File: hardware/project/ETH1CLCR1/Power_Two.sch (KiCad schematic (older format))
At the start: 53 parts, among them U1501 LT8330_S6, U1502 LT8330_S6, U1503 MC7815BD2TG, U1504 MC7915BD2TG, U1505 MC78M12ABDTRKG, U1506 MC79M12CDTG, U1507 TSR2-2450, U1508 TSR1-2490, U1509 LM1117IMP-3.3/NOPB, U1510 LM1117IMP-3.3/NOPB, U1511 LM1117IMP-5.0/NOPB

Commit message: PCB layout
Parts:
- R1506: value R -> 97k6
- R1508: value R -> 46k4
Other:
- moved on the sheet: C1501, C1502, C1503, C1504, C1505, C1506, C1507, C1508, C1509, C1510, C1511, C1512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

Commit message: Changes in schematics.
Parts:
- C1510, C1512: value 2u2/50V -> 4u7/50V
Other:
- moved on the sheet: TP1501
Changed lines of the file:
@@
 encoding utf-8
 Sheet 15 15
-Title ""
-Date ""
-Rev ""
+Title "Power supply second"
+Date "2020-01-19"
+Rev "1.0"
 Comp ""
-Comment1 ""
+Comment1 "Verification done."
 Comment2 ""
 Comment3 ""
@@
 Wire Wire Line
 	6500 1000 6550 1000
-Wire Wire Line
-	6550 1450 6550 1400
 $Comp
 L Device:R R1505
@@
 Wire Wire Line
 	6500 3350 6550 3350
-Wire Wire Line
-	6550 3800 6550 3750
 $Comp
 L Device:R R1507
@@
 P 8150 3800
 F 0 "C1510" H 8265 3846 50  0000 L CNN
-F 1 "2u2/50V" H 8265 3755 50  0000 L CNN
+F 1 "4u7/50V" H 8265 3755 50  0000 L CNN
 F 2 "Capacitor_SMD:C_1206_3216Metric_Pad1.42x1.75mm_HandSolder" H 8188 3650 50  0001 C CNN
 F 3 "~" H 8150 3800 50  0001 C CNN
@@
 P 8750 3800
 F 0 "C1512" H 8865 3846 50  0000 L CNN
-F 1 "2u2/50V" H 8865 3755 50  0000 L CNN
+F 1 "4u7/50V" H 8865 3755 50  0000 L CNN
 F 2 "Capacitor_SMD:C_1206_3216Metric_Pad1.42x1.75mm_HandSolder" H 8788 3650 50  0001 C CNN
 F 3 "~" H 8750 3800 50  0001 C CNN
@@
 L ETH1CLCR1:DGNDF #PWR01509
 U 1 1 5DF487C8
-P 6550 1450
-F 0 "#PWR01509" H 6550 1200 50  0001 C CNN
-F 1 "DGNDF" H 6555 1277 50  0000 C CNN
-F 2 "" H 6550 1450 50  0001 C CNN
-F 3 "" H 6550 1450 50  0001 C CNN
-	1    6550 1450
+P 6550 1400
+F 0 "#PWR01509" H 6550 1150 50  0001 C CNN
+F 1 "DGNDF" H 6555 1227 50  0000 C CNN
+F 2 "" H 6550 1400 50  0001 C CNN
+F 3 "" H 6550 1400 50  0001 C CNN
+	1    6550 1400
 	1    0    0    -1
 $EndComp
@@
 L ETH1CLCR1:DGNDF #PWR01510
 U 1 1 5F7AA41C
-P 6550 3800
-F 0 "#PWR01510" H 6550 3550 50  0001 C CNN
-F 1 "DGNDF" H 6555 3627 50  0000 C CNN
-F 2 "" H 6550 3800 50  0001 C CNN
-F 3 "" H 6550 3800 50  0001 C CNN
-	1    6550 3800
+P 6550 3750
+F 0 "#PWR01510" H 6550 3500 50  0001 C CNN
+F 1 "DGNDF" H 6555 3577 50  0000 C CNN
+F 2 "" H 6550 3750 50  0001 C CNN
+F 3 "" H 6550 3750 50  0001 C CNN
+	1    6550 3750
 	1    0    0    -1
 $EndComp
@@
 L Connector:TestPoint TP?
 U 1 1 5E1A35BB
-P 900 900
+P 900 800
 AR Path="/5DF36C0B/5E1A35BB" Ref="TP?"  Part="1"
 AR Path="/5DD0DBE6/5E1A35BB" Ref="TP?"  Part="1"
 AR Path="/5DEC0296/5E1A35BB" Ref="TP1501"  Part="1"
-F 0 "TP1501" H 958 1018 50  0000 L CNN
-F 1 "5006" H 958 927 50  0000 L CNN
-F 2 "TestPoint:TestPoint_Loop_D2.60mm_Drill1.6mm_Beaded" H 1100 900 50  0001 C CNN
-F 3 "~" H 1100 900 50  0001 C CNN
-	1    900  900
+F 0 "TP1501" H 958 918 50  0000 L CNN
+F 1 "5006" H 958 827 50  0000 L CNN
+F 2 "TestPoint:TestPoint_Loop_D2.60mm_Drill1.6mm_Beaded" H 1100 800 50  0001 C CNN
+F 3 "~" H 1100 800 50  0001 C CNN
+	1    900  800
 	1    0    0    -1
 $EndComp
@@
 L ETH1CLCR1:DGNDF #PWR01503
 U 1 1 5E1AEE0F
-P 900 1000
-F 0 "#PWR01503" H 900 750 50  0001 C CNN
-F 1 "DGNDF" H 905 827 50  0000 C CNN
-F 2 "" H 900 1000 50  0001 C CNN
-F 3 "" H 900 1000 50  0001 C CNN
-	1    900  1000
-	1    0    0    -1
-$EndComp
-Wire Wire Line
-	900  1000 900  900
+P 900 900
+F 0 "#PWR01503" H 900 650 50  0001 C CNN
+F 1 "DGNDF" H 905 727 50  0000 C CNN
+F 2 "" H 900 900 50  0001 C CNN
+F 3 "" H 900 900 50  0001 C CNN
+	1    900  900
+	1    0    0    -1
+$EndComp
+Wire Wire Line
+	900  900  900  800
 $Comp
 L power:PWR_FLAG #FLG01504
@@
 L ETH1CLCR1:+24VF #PWR01518
 U 1 1 5E91BD20
-P 3300 850
-F 0 "#PWR01518" H 3300 700 50  0001 C CNN
-F 1 "+24VF" H 3315 1023 50  0000 C CNN
-F 2 "" H 3300 850 50  0001 C CNN
-F 3 "" H 3300 850 50  0001 C CNN
-	1    3300 850
+P 2650 800
+F 0 "#PWR01518" H 2650 650 50  0001 C CNN
+F 1 "+24VF" H 2665 973 50  0000 C CNN
+F 2 "" H 2650 800 50  0001 C CNN
+F 3 "" H 2650 800 50  0001 C CNN
+	1    2650 800
 	1    0    0    -1
 $EndComp
@@
 L ETH1CLCR1:+24VDD #PWR01517
 U 1 1 5E91C38B
-P 2850 850
-F 0 "#PWR01517" H 2850 700 50  0001 C CNN
-F 1 "+24VDD" H 2865 1023 50  0000 C CNN
-F 2 "" H 2850 850 50  0001 C CNN
-F 3 "" H 2850 850 50  0001 C CNN
-	1    2850 850
-	1    0    0    -1
-$EndComp
-Wire Wire Line
-	2850 850  2850 900
-Wire Wire Line
-	2850 900  3300 900
-Wire Wire Line
-	3300 900  3300 850
+P 2200 800
+F 0 "#PWR01517" H 2200 650 50  0001 C CNN
+F 1 "+24VDD" H 2215 973 50  0000 C CNN
+F 2 "" H 2200 800 50  0001 C CNN
+F 3 "" H 2200 800 50  0001 C CNN
+	1    2200 800
+	1    0    0    -1
+$EndComp
+Wire Wire Line
+	2200 800  2200 850
+Wire Wire Line
+	2200 850  2650 850
+Wire Wire Line
+	2650 850  2650 800
 $Comp
 L ETH1CLCR1:DGNDF #PWR01504
 U 1 1 5E95CC6A
-P 1900 1000
-F 0 "#PWR01504" H 1900 750 50  0001 C CNN
-F 1 "DGNDF" H 1905 827 50  0000 C CNN
-F 2 "" H 1900 1000 50  0001 C CNN
-F 3 "" H 1900 1000 50  0001 C CNN
-	1    1900 1000
+P 1350 900
+F 0 "#PWR01504" H 1350 650 50  0001 C CNN
+F 1 "DGNDF" H 1355 727 50  0000 C CNN
+F 2 "" H 1350 900 50  0001 C CNN
+F 3 "" H 1350 900 50  0001 C CNN
+	1    1350 900
 	1    0    0    -1
 $EndComp
@@
 L ETH1CLCR1:AGNDF #PWR01505
 U 1 1 5E95D4F1
-P 2250 1000
-F 0 "#PWR01505" H 2250 750 50  0001 C CNN
-F 1 "AGNDF" H 2255 827 50  0000 C CNN
-F 2 "" H 2250 1000 50  0001 C CNN
-F 3 "" H 2250 1000 50  0001 C CNN
-	1    2250 1000
-	1    0    0    -1
-$EndComp
-Wire Wire Line
-	2250 1000 2250 950
-Wire Wire Line
-	2250 950  1900 950
-Wire Wire Line
-	1900 950  1900 1000
+P 1700 900
+F 0 "#PWR01505" H 1700 650 50  0001 C CNN
+F 1 "AGNDF" H 1705 727 50  0000 C CNN
+F 2 "" H 1700 900 50  0001 C CNN
+F 3 "" H 1700 900 50  0001 C CNN
+	1    1700 900
+	1    0    0    -1
+$EndComp
+Wire Wire Line
+	1700 900  1700 850
+Wire Wire Line
+	1700 850  1350 850
+Wire Wire Line
+	1350 850  1350 900
 $Comp
 L power:GND #PWR01508
 U 1 1 5EA5587E
-P 2600 1000
-F 0 "#PWR01508" H 2600 750 50  0001 C CNN
-F 1 "GND" H 2605 827 50  0000 C CNN
-F 2 "" H 2600 1000 50  0001 C CNN
-F 3 "" H 2600 1000 50  0001 C CNN
-	1    2600 1000
-	1    0    0    -1
-$EndComp
-Wire Wire Line
-	2250 950  2600 950
-Wire Wire Line
-	2600 950  2600 1000
-Connection ~ 2250 950
+P 2050 900
+F 0 "#PWR01508" H 2050 650 50  0001 C CNN
+F 1 "GND" H 2055 727 50  0000 C CNN
+F 2 "" H 2050 900 50  0001 C CNN
+F 3 "" H 2050 900 50  0001 C CNN
+	1    2050 900
+	1    0    0    -1
+$EndComp
+Wire Wire Line
+	1700 850  2050 850
+Wire Wire Line
+	2050 850  2050 900
+Connection ~ 1700 850
 $EndSCHEMATC

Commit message: Checked the schematics. Created BOM.
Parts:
- U1509, U1510: value LM1117IMP-3.3/NOPB -> LM1117DTX-3.3/NOPB
- U1511: value LM1117IMP-5.0/NOPB -> LM1117DTX-5.0/NOPB
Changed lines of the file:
@@
 AR Path="/5DEC0296/5DCFB96F" Ref="U1510"  Part="1"
 F 0 "U1510" H 3850 6942 50  0000 C CNN
-F 1 "LM1117IMP-3.3/NOPB" H 3850 6850 50  0000 C CNN
+F 1 "LM1117DTX-3.3/NOPB" H 3850 6850 50  0000 C CNN
 F 2 "Package_TO_SOT_SMD:TO-252-2" H 3850 6700 50  0001 C CNN
 F 3 "http://www.ti.com/lit/ds/symlink/lm1117.pdf" H 3850 6700 50  0001 C CNN
@@
 AR Path="/5DEC0296/5DED3D6D" Ref="U1511"  Part="1"
 F 0 "U1511" H 10150 5792 50  0000 C CNN
-F 1 "LM1117IMP-5.0/NOPB" H 10150 5700 50  0000 C CNN
+F 1 "LM1117DTX-5.0/NOPB" H 10150 5700 50  0000 C CNN
 F 2 "Package_TO_SOT_SMD:TO-252-2" H 10150 5550 50  0001 C CNN
 F 3 "http://www.ti.com/lit/ds/symlink/lm1117.pdf" H 10150 5550 50  0001 C CNN
@@
 AR Path="/5DEC0296/5E4B714B" Ref="U1509"  Part="1"
 F 0 "U1509" H 3850 5742 50  0000 C CNN
-F 1 "LM1117IMP-3.3/NOPB" H 3850 5650 50  0000 C CNN
+F 1 "LM1117DTX-3.3/NOPB" H 3850 5650 50  0000 C CNN
 F 2 "Package_TO_SOT_SMD:TO-252-2" H 3850 5500 50  0001 C CNN
 F 3 "http://www.ti.com/lit/ds/symlink/lm1117.pdf" H 3850 5500 50  0001 C CNN

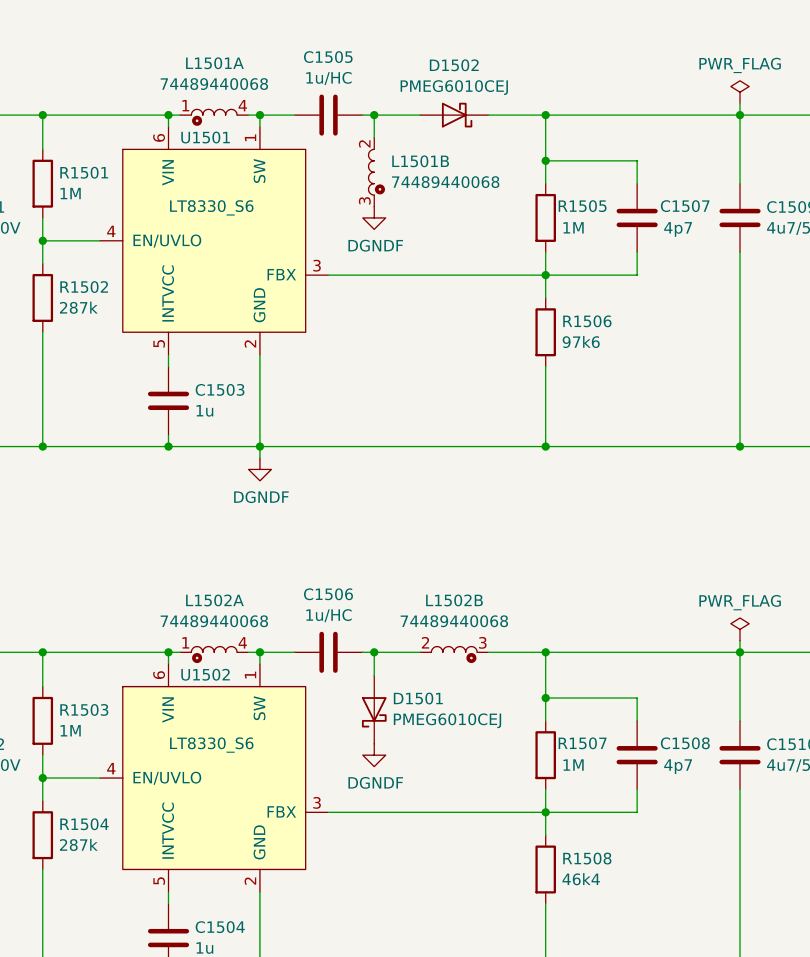
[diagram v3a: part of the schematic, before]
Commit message: Fixed some mistakes in the foorpeints. BOM list ready.
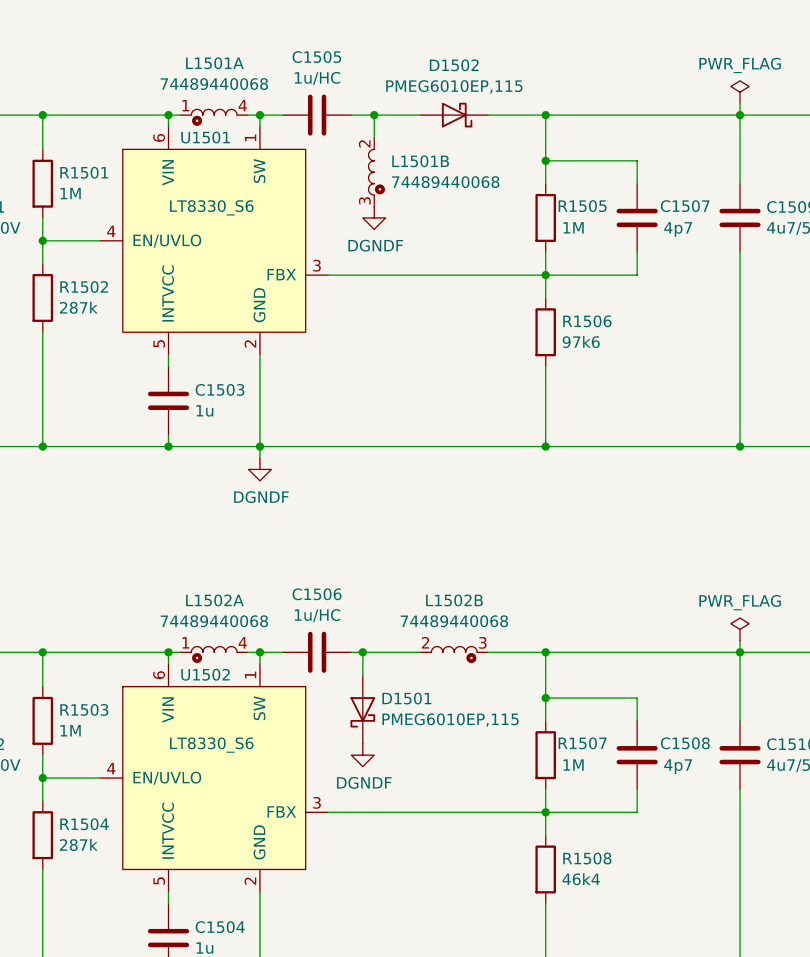
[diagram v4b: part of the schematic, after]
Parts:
- D1501, D1502: value PMEG6010CEJ -> PMEG6010EP,115; footprint Diode_SMD:D_SOD-323_HandSoldering -> Diode_SMD:D_SOD-128
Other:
- moved on the sheet: C1505, C1506, D1501
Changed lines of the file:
@@
 L Device:C C1505
 U 1 1 5DD4C41A
-P 6350 1000
-F 0 "C1505" V 6098 1000 50  0000 C CNN
-F 1 "1u/HC" V 6189 1000 50  0000 C CNN
-F 2 "Capacitor_SMD:C_1206_3216Metric_Pad1.42x1.75mm_HandSolder" H 6388 850 50  0001 C CNN
-F 3 "~" H 6350 1000 50  0001 C CNN
-	1    6350 1000
+P 6300 1000
+F 0 "C1505" V 6048 1000 50  0000 C CNN
+F 1 "1u/HC" V 6139 1000 50  0000 C CNN
+F 2 "Capacitor_SMD:C_1206_3216Metric_Pad1.42x1.75mm_HandSolder" H 6338 850 50  0001 C CNN
+F 3 "~" H 6300 1000 50  0001 C CNN
+	1    6300 1000
 	0    1    1    0
 $EndComp
 Wire Wire Line
-	6200 1000 6050 1000
+	6150 1000 6050 1000
 Connection ~ 6050 1000
 Wire Wire Line
 	6550 1100 6550 1000
 Wire Wire Line
-	6500 1000 6550 1000
+	6450 1000 6550 1000
 $Comp
 L Device:R R1505
@@
 P 6900 1000
 F 0 "D1502" H 6900 784 50  0000 C CNN
-F 1 "PMEG6010CEJ" H 6900 875 50  0000 C CNN
-F 2 "Diode_SMD:D_SOD-323_HandSoldering" H 6900 1000 50  0001 C CNN
+F 1 "PMEG6010EP,115" H 6900 875 50  0000 C CNN
+F 2 "Diode_SMD:D_SOD-128" H 6900 1000 50  0001 C CNN
 F 3 "~" H 6900 1000 50  0001 C CNN
 	1    6900 1000
@@
 	1    0    0    -1
 $EndComp
-$Comp
-L Device:C C1506
-U 1 1 5DE720A2
-P 6350 3350
-F 0 "C1506" V 6098 3350 50  0000 C CNN
-F 1 "1u/HC" V 6189 3350 50  0000 C CNN
-F 2 "Capacitor_SMD:C_1206_3216Metric_Pad1.42x1.75mm_HandSolder" H 6388 3200 50  0001 C CNN
-F 3 "~" H 6350 3350 50  0001 C CNN
-	1    6350 3350
-	0    1    1    0
-$EndComp
-Wire Wire Line
-	6200 3350 6050 3350
 Connection ~ 6050 3350
-Wire Wire Line
-	6550 3450 6550 3350
-Wire Wire Line
-	6500 3350 6550 3350
 $Comp
 L Device:R R1507
@@
 Connection ~ 8150 4800
 $Comp
-L Device:D_Schottky D1501
-U 1 1 5DE720D1
-P 6550 3600
-F 0 "D1501" V 6596 3521 50  0000 R CNN
-F 1 "PMEG6010CEJ" V 6505 3521 50  0000 R CNN
-F 2 "Diode_SMD:D_SOD-323_HandSoldering" H 6550 3600 50  0001 C CNN
-F 3 "~" H 6550 3600 50  0001 C CNN
-	1    6550 3600
-	0    -1   -1   0
-$EndComp
-$Comp
 L Device:C C1502
 U 1 1 5DE720D7
@@
 Wire Wire Line
 	9800 3300 9800 3350
-Connection ~ 6550 3350
-Wire Wire Line
-	6550 3350 6750 3350
 Wire Wire Line
 	7300 4800 6050 4800
@@
 Connection ~ 4350 5500
 $Comp
-L ETH1CLCR1:DGNDF #PWR01510
-U 1 1 5F7AA41C
-P 6550 3750
-F 0 "#PWR01510" H 6550 3500 50  0001 C CNN
-F 1 "DGNDF" H 6555 3577 50  0000 C CNN
-F 2 "" H 6550 3750 50  0001 C CNN
-F 3 "" H 6550 3750 50  0001 C CNN
-	1    6550 3750
-	1    0    0    -1
-$EndComp
-$Comp
 L ETH1CLCR1:TSR2 U1507
 U 1 1 5DE430A3
@@
 	2050 850  2050 900
 Connection ~ 1700 850
+Wire Wire Line
+	6150 3350 6050 3350
+$Comp
+L Device:C C1506
+U 1 1 5DE720A2
+P 6300 3350
+F 0 "C1506" V 6048 3350 50  0000 C CNN
+F 1 "1u/HC" V 6139 3350 50  0000 C CNN
+F 2 "Capacitor_SMD:C_1206_3216Metric_Pad1.42x1.75mm_HandSolder" H 6338 3200 50  0001 C CNN
+F 3 "~" H 6300 3350 50  0001 C CNN
+	1    6300 3350
+	0    1    1    0
+$EndComp
+Wire Wire Line
+	6450 3350 6500 3350
+$Comp
+L ETH1CLCR1:DGNDF #PWR01510
+U 1 1 5F7AA41C
+P 6500 3750
+F 0 "#PWR01510" H 6500 3500 50  0001 C CNN
+F 1 "DGNDF" H 6505 3577 50  0000 C CNN
+F 2 "" H 6500 3750 50  0001 C CNN
+F 3 "" H 6500 3750 50  0001 C CNN
+	1    6500 3750
+	1    0    0    -1
+$EndComp
+$Comp
+L Device:D_Schottky D1501
+U 1 1 5DE720D1
+P 6500 3600
+F 0 "D1501" V 6546 3521 50  0000 R CNN
+F 1 "PMEG6010EP,115" V 6455 3521 50  0000 R CNN
+F 2 "Diode_SMD:D_SOD-128" H 6500 3600 50  0001 C CNN
+F 3 "~" H 6500 3600 50  0001 C CNN
+	1    6500 3600
+	0    -1   -1   0
+$EndComp
+Wire Wire Line
+	6500 3450 6500 3350
+Connection ~ 6500 3350
+Wire Wire Line
+	6500 3350 6750 3350
 $EndSCHEMATC

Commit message: PCB layout
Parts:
- added C1506, C1507: 10u/50V, Capacitor_SMD:C_1206_3216Metric_Pad1.42x1.75mm_HandSolder, symbol Device:C
- renumbered C1517 to C1501, C1518 to C1502, C1520 to C1503, C1522 to C1504, C1523 to C1505, C1525 to C1508, C1526 to C1509, C1501 to C1510, C1502 to C1511, C1503 to C1512, C1504 to C1513, C1505 to C1514, C1506 to C1515, C1507 to C1516, C1508 to C1517, C1519 to C1518, C1509 to C1519, C1510 to C1520, C1511 to C1522, C1512 to C1523, C1513 to C1524, C1514 to C1525, C1524 to C1526, C1515 to C1527, C1516 to C1528, C1527 to C1529, L1503 to L1501, L1501 to L1502, L1502 to L1503, U1507 to U1501, U1509 to U1502, U1510 to U1503, U1501 to U1504, U1502 to U1505, U1503 to U1506, U1504 to U1507, U1511 to U1509, U1505 to U1510, U1506 to U1511
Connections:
- net +24VDD: now also C1506.1, C1507.1
- net AGNDF: now also C1506.2, C1507.2
